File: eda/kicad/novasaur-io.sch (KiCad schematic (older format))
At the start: 67 parts, among them J1 POWER IN, J3 AUDIO OUT, J4 KEYBOARD, J5 SERIAL, J5 SPKR, J6 DISPLAY, J7 EXPANSION, J8 EXP OUT, Q1 2N3904, Q2 2N3904, Q4 BS270, U1 74F86, U2 74F08, U38 74HCT4053, U39 MAX232, U4 74F32, U40 NJM4580, U41 LM2576, U6 74ALS139, U7 74ALS139

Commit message: final rev5 update before removing buck reg
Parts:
- RN7, RN8: footprint Resistor_THT:R_Array_SIP8 -> Resistor_THT:R_Array_SIP9; symbol Device:R_Network07_US -> Device:R_Network08_US
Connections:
- wire segments 351 -> 353
- no-connect marks 9 -> 11
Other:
- moved on the sheet: RN9
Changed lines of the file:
@@
 L Device:R_Pack03_SIP RN?
 U 1 1 5F52EE33
-P 4300 3800
+P 4300 3900
 AR Path="/5DAA3954/5F52EE33" Ref="RN?"  Part="1"
 AR Path="/5F52EE33" Ref="RN?"  Part="1"
@@
 AR Path="/5DA1E9BD/5F52EE33" Ref="RN?"  Part="1"
 AR Path="/5DA1E9C0/5F52EE33" Ref="RN9"  Part="1"
-F 0 "RN9" V 3750 3750 50  0000 L CNN
-F 1 "220" V 3850 3750 50  0000 L CNN
-F 2 "Resistor_THT:R_Array_SIP6" V 4875 3800 50  0001 C CNN
-F 3 "http://www.vishay.com/docs/31509/csc.pdf" H 4300 3800 50  0001 C CNN
-	1    4300 3800
+F 0 "RN9" V 3750 3850 50  0000 L CNN
+F 1 "220" V 3850 3850 50  0000 L CNN
+F 2 "Resistor_THT:R_Array_SIP6" V 4875 3900 50  0001 C CNN
+F 3 "http://www.vishay.com/docs/31509/csc.pdf" H 4300 3900 50  0001 C CNN
+	1    4300 3900
 	0    -1   1    0
 $EndComp
 Wire Wire Line
-	4550 2650 4450 2650
-Wire Wire Line
-	4550 2550 4450 2550
-Wire Wire Line
-	4450 2950 4550 2950
-Wire Wire Line
-	4550 2850 4450 2850
+	4550 2700 4450 2700
+Wire Wire Line
+	4550 2600 4450 2600
+Wire Wire Line
+	4450 3000 4550 3000
+Wire Wire Line
+	4550 2900 4450 2900
 Wire Wire Line
 	4550 1500 4450 1500
@@
 	4450 1900 4550 1900
 Wire Wire Line
-	4550 2650 4550 2600
+	4550 2700 4550 2650
 Wire Wire Line
 	4450 1800 4550 1800
 Wire Wire Line
+	4500 4000 4550 4000
+Wire Wire Line
+	4550 4000 4550 4200
+Wire Wire Line
+	4550 4200 4500 4200
+Wire Wire Line
 	4500 3900 4550 3900
 Wire Wire Line
-	4550 3900 4550 4100
-Wire Wire Line
-	4550 4100 4500 4100
-Wire Wire Line
-	4500 3800 4550 3800
-Wire Wire Line
-	4500 3600 4550 3600
-Wire Wire Line
-	4550 3600 4550 3800
-Text Label 4600 3500 0    50   ~ 0
+	4500 3700 4550 3700
+Wire Wire Line
+	4550 3700 4550 3900
+Text Label 4600 3600 0    50   ~ 0
 C6
-Text Label 4600 4200 0    50   ~ 0
+Text Label 4600 4300 0    50   ~ 0
 C7
 Text Label 4600 1400 0    50   ~ 0
@@
 Text Label 4600 1700 0    50   ~ 0
 C2
-Text Label 4600 2450 0    50   ~ 0
+Text Label 4600 2500 0    50   ~ 0
 C3
-Text Label 4600 2600 0    50   ~ 0
+Text Label 4600 2650 0    50   ~ 0
 C4
-Text Label 4600 2750 0    50   ~ 0
+Text Label 4600 2800 0    50   ~ 0
 C5
 Wire Wire Line
@@
 Wire Wire Line
 	4550 1550 4550 1500
-Connection ~ 4550 2600
-Wire Wire Line
-	4550 2600 4550 2550
-Wire Wire Line
-	4550 2850 4550 2950
-Wire Wire Line
-	4550 2850 4550 2750
-Connection ~ 4550 2850
-Wire Wire Line
-	4450 3050 4550 3050
-Wire Wire Line
-	4550 3050 4550 2950
-Connection ~ 4550 2950
-Wire Wire Line
-	4700 3500 4500 3500
-Wire Wire Line
-	4700 4200 4500 4200
+Connection ~ 4550 2650
+Wire Wire Line
+	4550 2650 4550 2600
+Wire Wire Line
+	4550 2900 4550 3000
+Wire Wire Line
+	4550 2900 4550 2800
+Connection ~ 4550 2900
+Wire Wire Line
+	4450 3100 4550 3100
+Wire Wire Line
+	4550 3100 4550 3000
+Connection ~ 4550 3000
+Wire Wire Line
+	4700 3600 4500 3600
+Wire Wire Line
+	4700 4300 4500 4300
 Wire Wire Line
 	4700 1550 4550 1550
@@
 	4700 1700 4550 1700
 Wire Wire Line
-	4700 2600 4550 2600
-Entry Wire Line
-	4700 3500 4800 3400
-Entry Wire Line
-	4700 4200 4800 4100
+	4700 2650 4550 2650
+Entry Wire Line
+	4700 3600 4800 3500
+Entry Wire Line
+	4700 4300 4800 4200
 Entry Wire Line
 	4800 1450 4700 1550
@@
 	4800 1600 4700 1700
 Entry Wire Line
-	4800 2350 4700 2450
-Entry Wire Line
-	4800 2650 4700 2750
-Entry Wire Line
-	4800 2500 4700 2600
-Connection ~ 4550 4100
+	4800 2400 4700 2500
+Entry Wire Line
+	4800 2700 4700 2800
+Entry Wire Line
+	4800 2550 4700 2650
+Connection ~ 4550 4200
 Text GLabel 4800 1100 1    50   Input ~ 0
 C[0..7]
@@
 	4450 1400 4700 1400
 Wire Wire Line
-	4450 2450 4700 2450
-Wire Wire Line
-	4550 2750 4700 2750
+	4450 2500 4700 2500
+Wire Wire Line
+	4550 2800 4700 2800
 Wire Wire Line
 	4450 1700 4550 1700
 Connection ~ 4550 1700
 Wire Wire Line
-	4450 2750 4550 2750
-Connection ~ 4550 2750
+	4450 2800 4550 2800
+Connection ~ 4550 2800
 $Comp
 L power:GNDD #PWR?
@@
 	8250 4350 8250 4100
 $Comp
-L Device:R_Network07_US RN?
+L Device:R_Network08_US RN?
 U 1 1 5DF0AA91
-P 4250 1700
+P 4250 1800
 AR Path="/5DAA3954/5DF0AA91" Ref="RN?"  Part="1"
 AR Path="/5DAA5CD8/5D9A6C5F/5DF0AA91" Ref="RN?"  Part="1"
 AR Path="/5DA1E9BD/5DF0AA91" Ref="RN?"  Part="1"
 AR Path="/5DA1E9C0/5DF0AA91" Ref="RN7"  Part="1"
-F 0 "RN7" V 3700 1600 50  0000 L CNN
-F 1 "1k" V 3800 1650 50  0000 L CNN
-F 2 "Resistor_THT:R_Array_SIP8" V 4725 1700 50  0001 C CNN
-F 3 "http://www.vishay.com/docs/31509/csc.pdf" H 4250 1700 50  0001 C CNN
-	1    4250 1700
+F 0 "RN7" V 3600 1700 50  0000 L CNN
+F 1 "1k" V 3700 1750 50  0000 L CNN
+F 2 "Resistor_THT:R_Array_SIP9" V 4725 1800 50  0001 C CNN
+F 3 "http://www.vishay.com/docs/31509/csc.pdf" H 4250 1800 50  0001 C CNN
+	1    4250 1800
 	0    -1   1    0
 $EndComp
 $Comp
-L Device:R_Network07_US RN?
+L Device:R_Network08_US RN?
 U 1 1 5DF28750
-P 4250 2750
+P 4250 2900
 AR Path="/5DAA3954/5DF28750" Ref="RN?"  Part="1"
 AR Path="/5DAA5CD8/5D9A6C5F/5DF28750" Ref="RN?"  Part="1"
 AR Path="/5DA1E9BD/5DF28750" Ref="RN?"  Part="1"
 AR Path="/5DA1E9C0/5DF28750" Ref="RN8"  Part="1"
-F 0 "RN8" V 3700 2650 50  0000 L CNN
-F 1 "1k" V 3800 2700 50  0000 L CNN
-F 2 "Resistor_THT:R_Array_SIP8" V 4725 2750 50  0001 C CNN
-F 3 "http://www.vishay.com/docs/31509/csc.pdf" H 4250 2750 50  0001 C CNN
-	1    4250 2750
+F 0 "RN8" V 3600 2800 50  0000 L CNN
+F 1 "1k" V 3700 2850 50  0000 L CNN
+F 2 "Resistor_THT:R_Array_SIP9" V 4725 2900 50  0001 C CNN
+F 3 "http://www.vishay.com/docs/31509/csc.pdf" H 4250 2900 50  0001 C CNN
+	1    4250 2900
 	0    -1   1    0
 $EndComp
@@
 	3900 6650 4200 6650
 Wire Wire Line
-	4550 4100 4550 4350
-Wire Wire Line
-	4050 2450 3950 2450
+	4050 2500 3950 2500
 Wire Wire Line
 	4050 1400 3750 1400
@@
 	3600 3750 3750 3750
 Wire Wire Line
-	3600 4050 3950 4050
-Wire Wire Line
-	3600 4350 4550 4350
-Wire Wire Line
-	3950 2450 3950 4050
+	3950 2500 3950 4050
 Wire Wire Line
 	1600 2400 1650 2400
@@
 	8000 1050 8200 1050
 Connection ~ 8000 1300
+NoConn ~ 4450 2100
+NoConn ~ 4450 3200
+Wire Wire Line
+	3600 4050 3950 4050
+Wire Wire Line
+	3950 4350 3600 4350
+Wire Wire Line
+	3950 4550 4550 4550
+Wire Wire Line
+	4550 4200 4550 4550
+Wire Wire Line
+	3950 4350 3950 4550
 Wire Bus Line
 	4300 6750 4300 7050
@@
 	4950 1100 4950 2000
 Wire Bus Line
-	4800 1100 4800 4100
+	2850 1400 2850 2200
 Wire Bus Line
-	2850 1400 2850 2200
+	4800 1100 4800 4200
 $EndSCHEMATC

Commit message: rev5 schematic
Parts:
- removed C13: 1000u, Capacitor_THT:CP_Radial_D10.0mm_P5.00mm, symbol Device:CP1
- removed C23: 100u, Capacitor_THT:CP_Radial_D8.0mm_P3.50mm, symbol Device:CP1
- removed D3: 1N5822, Diode_THT:D_DO-201AD_P5.08mm_Vertical_AnodeUp, symbol Device:D_Schottky_ALT
- removed L1: 180uH, Inductor_THT:L_Radial_D12.5mm_P7.00mm_Fastron_09HCP, symbol Device:L_Core_Ferrite
- removed TP35: +24v, TestPoint:TestPoint_THTPad_1.0x1.0mm_Drill0.5mm, symbol Connector:TestPoint_Alt
- removed U41: LM2576, Package_TO_SOT_THT:TO-220-5_P3.4x3.7mm_StaggerOdd_Lead3.8mm_Vertical, symbol Regulator_Switching:LM2576HVT-5
- added C22, C23: 4.7u, Capacitor_THT:C_Disc_D6.0mm_W4.4mm_P5.00mm, symbol Device:C
- added U41: MCP1827S, Package_TO_SOT_THT:TO-220-3_Horizontal_TabDown, symbol Regulator_Linear:MCP1826S
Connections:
- net labels removed: +24V
- wire segments 353 -> 338
- no-connect marks 11 -> 12
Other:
- moved on the sheet: C1, C2, C3, C4, C5, J1, TP33, TP34, U1E, U2E, U3E, U4C

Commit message: rev 1.6 schematic
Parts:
- U41: footprint Package_TO_SOT_THT:TO-220-3_Horizontal_TabDown -> Package_TO_SOT_THT:TO-220-5_P3.4x3.8mm_StaggerOdd_Lead7.13mm_TabDown; symbol Regulator_Linear:MCP1826S -> Regulator_Linear:LP3963-3.3
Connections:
- net labels added: ~reset
- wire segments 338 -> 339
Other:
- moved on the sheet: C1, C2, C22, C23, C3, C4, C5, J1, TP33, TP34

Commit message: rename P reg to T
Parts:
- C22: renamed from C23; value 4.7u -> 1u; footprint Capacitor_THT:C_Disc_D6.0mm_W4.4mm_P5.00mm -> Capacitor_THT:C_Disc_D5.1mm_W3.2mm_P5.00mm
- C23: renamed from C22; value 4.7u -> 22u; footprint Capacitor_THT:C_Disc_D6.0mm_W4.4mm_P5.00mm -> Capacitor_THT:CP_Radial_D6.3mm_P2.50mm; symbol Device:C -> Device:CP1
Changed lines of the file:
@@
 Sheet 4 4
 Title "Input & Output"
-Date "2020-03-08"
+Date "2020-03-29"
 Rev "1.6"
 Comp ""
@@
 AR Path="/5DAA5CD8/5D9AFF37/630964B4" Ref="C?"  Part="1"
 AR Path="/5DA1E9C0/630964B4" Ref="C19"  Part="1"
-F 0 "C19" H 7100 2150 50  0000 C CNN
-F 1 "330p" H 7100 2050 50  0000 C CNN
+F 0 "C19" H 7150 2150 50  0000 C CNN
+F 1 "330p" H 7150 2050 50  0000 C CNN
 F 2 "Capacitor_THT:C_Disc_D3.0mm_W2.0mm_P2.50mm" H 6938 1950 50  0001 C CNN
 F 3 "~" H 6900 2100 50  0001 C CNN
@@
 AR Path="/5DAA5CD8/5D9AFF37/5EAB34C5" Ref="C?"  Part="1"
 AR Path="/5DA1E9C0/5EAB34C5" Ref="C18"  Part="1"
-F 0 "C18" H 6300 2150 50  0000 C CNN
-F 1 "330p" H 6300 2050 50  0000 C CNN
+F 0 "C18" H 6350 2150 50  0000 C CNN
+F 1 "330p" H 6350 2050 50  0000 C CNN
 F 2 "Capacitor_THT:C_Disc_D3.0mm_W2.0mm_P2.50mm" H 6138 1950 50  0001 C CNN
 F 3 "~" H 6100 2100 50  0001 C CNN
@@
 AR Path="/5DAA5CD8/5D9AFF37/5E5DCFF5" Ref="R?"  Part="1"
 AR Path="/5DA1E9C0/5E5DCFF5" Ref="R8"  Part="1"
-F 0 "R8" H 8500 2100 50  0000 L CNN
+F 0 "R8" H 8550 2100 50  0000 L CNN
 F 1 "100k" H 8500 2000 50  0000 L CNN
 F 2 "Resistor_THT:R_Axial_DIN0204_L3.6mm_D1.6mm_P7.62mm_Horizontal" V 8440 2040 50  0001 C CNN
@@
 	9050 4100 9050 4350
 $Comp
-L Device:C C?
+L Device:CP1 C?
 U 1 1 5E710149
 P 7050 3650
 AR Path="/62D13D9D/5E710149" Ref="C?"  Part="1"
 AR Path="/5DAA5CD8/5D9AFF37/5E710149" Ref="C?"  Part="1"
-AR Path="/5DA1E9C0/5E710149" Ref="C22"  Part="1"
-F 0 "C22" H 7165 3696 50  0000 L CNN
-F 1 "4.7u" H 7165 3605 50  0000 L CNN
-F 2 "Capacitor_THT:C_Disc_D6.0mm_W4.4mm_P5.00mm" H 7088 3500 50  0001 C CNN
+AR Path="/5DA1E9C0/5E710149" Ref="C23"  Part="1"
+F 0 "C23" H 7165 3696 50  0000 L CNN
+F 1 "22u" H 7165 3605 50  0000 L CNN
+F 2 "Capacitor_THT:CP_Radial_D6.3mm_P2.50mm" H 7088 3500 50  0001 C CNN
 F 3 "~" H 7050 3650 50  0001 C CNN
 	1    7050 3650
@@
 AR Path="/62D13D9D/5E72DE16" Ref="C?"  Part="1"
 AR Path="/5DAA5CD8/5D9AFF37/5E72DE16" Ref="C?"  Part="1"
-AR Path="/5DA1E9C0/5E72DE16" Ref="C23"  Part="1"
-F 0 "C23" H 8765 3696 50  0000 L CNN
-F 1 "4.7u" H 8765 3605 50  0000 L CNN
-F 2 "Capacitor_THT:C_Disc_D6.0mm_W4.4mm_P5.00mm" H 8688 3500 50  0001 C CNN
+AR Path="/5DA1E9C0/5E72DE16" Ref="C22"  Part="1"
+F 0 "C22" H 8765 3696 50  0000 L CNN
+F 1 "1u" H 8765 3605 50  0000 L CNN
+F 2 "Capacitor_THT:C_Disc_D5.1mm_W3.2mm_P5.00mm" H 8688 3500 50  0001 C CNN
 F 3 "~" H 8650 3650 50  0001 C CNN
 	1    8650 3650

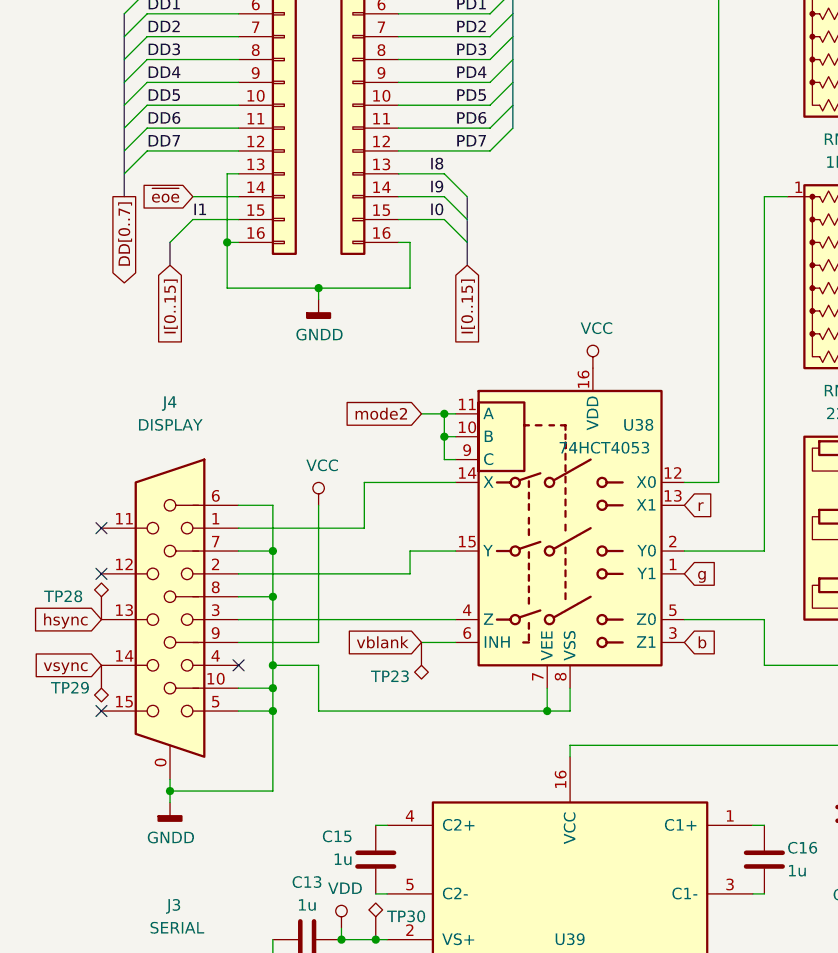
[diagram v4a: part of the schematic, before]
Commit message: add video headers
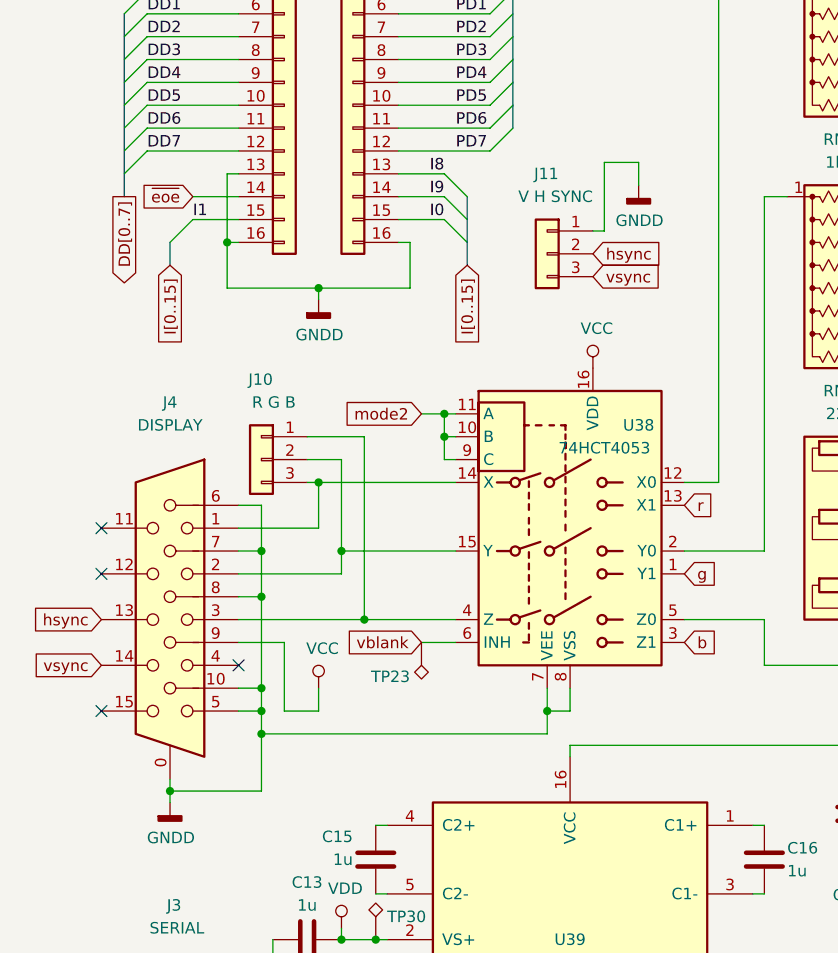
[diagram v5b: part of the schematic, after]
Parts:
- removed TP28: HSYNC, TestPoint:TestPoint_Pad_1.0x1.0mm, symbol Connector:TestPoint_Alt
- removed TP29: VSYNC, TestPoint:TestPoint_Pad_1.0x1.0mm, symbol Connector:TestPoint_Alt
- added J10: R G B, Connector_PinHeader_2.54mm:PinHeader_1x03_P2.54mm_Vertical, symbol Connector_Generic:Conn_01x03
- added J11: V H SYNC, Connector_PinHeader_2.54mm:PinHeader_1x03_P2.54mm_Vertical, symbol Connector_Generic:Conn_01x03
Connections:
- net GNDD: now also J11.1 (Pin_1)
- net hsync: now also J11.2 (Pin_2)
- net vsync: now also J11.3 (Pin_3)
- net at J6.1, U38.14 (X): now also J10.3 (Pin_3)
- net at J6.2, U38.15 (Y): now also J10.2 (Pin_2)
- net at J6.3, U38.4 (Z): now also J10.1 (Pin_1)
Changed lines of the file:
@@
 encoding utf-8
 Sheet 4 4
-Title "Input & Output"
-Date "2020-03-29"
+Title "Novasaur Retrocomputer"
+Date "2020-03-31"
 Rev "1.6"
 Comp ""
@@
 L power:VCC #PWR0115
 U 1 1 5D70CEC0
-P 2000 3850
+P 2000 4650
 AR Path="/62D13D9D/5D70CEC0" Ref="#PWR0115"  Part="1"
 AR Path="/5DAA5CD8/5D9AFF37/5D70CEC0" Ref="#PWR?"  Part="1"
 AR Path="/5DA1E9C0/5D70CEC0" Ref="#PWR0185"  Part="1"
-F 0 "#PWR0185" H 2000 3700 50  0001 C CNN
-F 1 "VCC" H 2017 4023 50  0000 C CNN
-F 2 "" H 2000 3850 50  0001 C CNN
-F 3 "" H 2000 3850 50  0001 C CNN
-	1    2000 3850
-	1    0    0    -1
-$EndComp
-Wire Wire Line
-	1650 4150 2400 4150
+F 0 "#PWR0185" H 2000 4500 50  0001 C CNN
+F 1 "VCC" H 2017 4823 50  0000 C CNN
+F 2 "" H 2000 4650 50  0001 C CNN
+F 3 "" H 2000 4650 50  0001 C CNN
+	1    2000 4650
+	1    0    0    -1
+$EndComp
 $Comp
 L Connector:DB15_Female_HighDensity_MountingHoles J6
@@
 	-1   0    0    -1
 $EndComp
-Wire Wire Line
-	1650 3950 2200 3950
 $Comp
 L Connector_Generic:Conn_01x16 J8
@@
 	2350 2300 2750 2300
 Wire Wire Line
-	2400 4150 2400 4050
-Wire Wire Line
-	2400 4050 2600 4050
-Wire Wire Line
-	2200 3950 2200 3750
-Wire Wire Line
-	2200 3750 2600 3750
-Wire Wire Line
 	1600 1200 1600 1100
 Wire Wire Line
@@
 Text GLabel 2450 3450 0    50   Input ~ 0
 mode2
-Connection ~ 2550 3450
 $Comp
 L Connector_Generic:Conn_01x16 J7
@@
 	1    0    0    -1
 $EndComp
-Wire Wire Line
-	2450 3450 2550 3450
 Wire Wire Line
 	1600 2700 1650 2700
@@
 	2050 6050 2100 6050
 Wire Wire Line
-	1650 4350 2600 4350
-Wire Wire Line
-	1650 3850 1800 3850
-Wire Wire Line
-	1650 4050 1800 4050
-Wire Wire Line
-	1650 4250 1800 4250
-Wire Wire Line
-	1650 4650 1800 4650
-Wire Wire Line
-	1650 4750 1800 4750
+	1650 3850 1750 3850
+Wire Wire Line
+	1650 4050 1750 4050
+Wire Wire Line
+	1650 4250 1750 4250
+Wire Wire Line
+	1650 4650 1750 4650
+Wire Wire Line
+	1650 4750 1750 4750
 Wire Wire Line
 	1350 5050 1350 5100
@@
 Wire Wire Line
 	1350 5100 1350 5150
-Wire Wire Line
-	1800 5100 1800 4750
-Wire Wire Line
-	1800 5100 1350 5100
-Connection ~ 1800 4750
-Wire Wire Line
-	1800 4650 1800 4550
-Connection ~ 1800 4650
-Connection ~ 1800 4250
-Wire Wire Line
-	1800 4250 1800 4050
-Connection ~ 1800 4050
-Wire Wire Line
-	1800 4050 1800 3850
-Wire Wire Line
-	1800 4750 1800 4650
-Wire Wire Line
-	1800 4550 2000 4550
-Connection ~ 1800 4550
-Wire Wire Line
-	1800 4250 1800 4550
-Wire Wire Line
-	2000 4750 3000 4750
 Connection ~ 3000 4750
 Wire Wire Line
@@
 Wire Wire Line
 	3000 4650 3000 4750
-Wire Wire Line
-	2000 4550 2000 4750
 $Comp
 L Device:C C?
@@
 Wire Wire Line
 	2100 6050 2250 6050
-$Comp
-L Connector:TestPoint_Alt TP?
-U 1 1 5E74D438
-P 1050 4350
-AR Path="/5E74D438" Ref="TP?"  Part="1"
-AR Path="/5DA1E9BA/5E74D438" Ref="TP?"  Part="1"
-AR Path="/5DA1E9BD/5E74D438" Ref="TP?"  Part="1"
-AR Path="/5DA1E9C0/5E74D438" Ref="TP28"  Part="1"
-F 0 "TP28" H 800 4450 50  0000 L CNN
-F 1 "HSYNC" H 800 4500 50  0001 L CNN
-F 2 "TestPoint:TestPoint_Pad_1.0x1.0mm" H 1250 4350 50  0001 C CNN
-F 3 "~" H 1250 4350 50  0001 C CNN
-	1    1050 4350
-	1    0    0    -1
-$EndComp
 Wire Wire Line
 	2300 5750 2250 5750
@@
 Wire Wire Line
 	6250 5000 6250 4900
-Wire Wire Line
-	2000 4450 2000 3850
-Wire Wire Line
-	1650 4450 2000 4450
 Entry Wire Line
 	1150 1400 1250 1500
@@
 	1250 1500 1650 1500
 $Comp
-L Connector:TestPoint_Alt TP?
-U 1 1 5E6FA207
-P 1050 4550
-AR Path="/5E6FA207" Ref="TP?"  Part="1"
-AR Path="/5DA1E9BA/5E6FA207" Ref="TP?"  Part="1"
-AR Path="/5DA1E9BD/5E6FA207" Ref="TP?"  Part="1"
-AR Path="/5DA1E9C0/5E6FA207" Ref="TP29"  Part="1"
-F 0 "TP29" H 1100 4650 50  0000 L CNN
-F 1 "VSYNC" H 800 4700 50  0001 L CNN
-F 2 "TestPoint:TestPoint_Pad_1.0x1.0mm" H 1250 4550 50  0001 C CNN
-F 3 "~" H 1250 4550 50  0001 C CNN
-	1    1050 4550
-	-1   0    0    1
-$EndComp
-$Comp
 L Transistor_BJT:2N3904 Q1
 U 1 1 5E7F79E8
@@
 Text GLabel 7450 3300 0    50   Output ~ 0
 ~reset
+$Comp
+L Connector_Generic:Conn_01x03 J10
+U 1 1 5E8D84F1
+P 1750 3650
+AR Path="/5DA1E9C0/5E8D84F1" Ref="J10"  Part="1"
+AR Path="/5E8D84F1" Ref="J?"  Part="1"
+F 0 "J10" H 1700 4000 50  0000 L CNN
+F 1 "R  G  B" H 1600 3900 50  0000 L CNN
+F 2 "Connector_PinHeader_2.54mm:PinHeader_1x03_P2.54mm_Vertical" H 1750 3650 50  0001 C CNN
+F 3 "~" H 1750 3650 50  0001 C CNN
+	1    1750 3650
+	-1   0    0    -1
+$EndComp
+Wire Wire Line
+	3000 4850 3000 4750
+Wire Wire Line
+	2550 3450 2450 3450
+Connection ~ 2550 3450
+Wire Wire Line
+	1650 4350 2200 4350
+Wire Wire Line
+	1650 3950 2000 3950
+Wire Wire Line
+	1650 4150 2100 4150
+Wire Wire Line
+	2000 3750 2000 3950
+Wire Wire Line
+	2000 3750 2600 3750
+Wire Wire Line
+	1950 3550 2200 3550
+Wire Wire Line
+	1950 3650 2100 3650
+Wire Wire Line
+	1950 3750 2000 3750
+Connection ~ 2000 3750
+Wire Wire Line
+	1750 3850 1750 4050
+Connection ~ 1750 4050
+Wire Wire Line
+	1750 4050 1750 4250
+Connection ~ 1750 4250
+Wire Wire Line
+	1750 4250 1750 4650
+Connection ~ 1750 4650
+Wire Wire Line
+	1750 4650 1750 4750
+Connection ~ 1750 4750
+Wire Wire Line
+	1750 4750 1750 4850
+Wire Wire Line
+	1750 4850 1750 5100
+Connection ~ 1750 4850
+Wire Wire Line
+	1750 5100 1350 5100
+Wire Wire Line
+	1750 4850 3000 4850
+Wire Wire Line
+	1650 4450 1850 4450
+Wire Wire Line
+	2100 3650 2100 4050
+Connection ~ 2100 4050
+Wire Wire Line
+	2100 4050 2100 4150
+Wire Wire Line
+	2100 4050 2600 4050
+Wire Wire Line
+	2200 3550 2200 4350
+Connection ~ 2200 4350
+Wire Wire Line
+	2200 4350 2600 4350
+Wire Wire Line
+	1850 4750 2000 4750
+Wire Wire Line
+	2000 4750 2000 4650
+Wire Wire Line
+	1850 4450 1850 4750
+Text GLabel 3200 2850 2    50   Input ~ 0
+vsync
+Text GLabel 3200 2750 2    50   Input ~ 0
+hsync
+Wire Wire Line
+	3400 2350 3400 2450
+$Comp
+L power:GNDD #PWR?
+U 1 1 5F8B73E5
+P 3400 2450
+AR Path="/62D13D9D/5F8B73E5" Ref="#PWR?"  Part="1"
+AR Path="/5DAA5CD8/5D9AFF37/5F8B73E5" Ref="#PWR?"  Part="1"
+AR Path="/5DA1E9C0/5F8B73E5" Ref="#PWR0181"  Part="1"
+F 0 "#PWR0181" H 3400 2200 50  0001 C CNN
+F 1 "GNDD" H 3404 2295 50  0000 C CNN
+F 2 "" H 3400 2450 50  0001 C CNN
+F 3 "" H 3400 2450 50  0001 C CNN
+	1    3400 2450
+	1    0    0    -1
+$EndComp
+Wire Wire Line
+	3200 2650 3250 2650
+Wire Wire Line
+	3250 2350 3400 2350
+Wire Wire Line
+	3250 2650 3250 2350
+$Comp
+L Connector_Generic:Conn_01x03 J11
+U 1 1 5F873810
+P 3000 2750
+AR Path="/5DA1E9C0/5F873810" Ref="J11"  Part="1"
+AR Path="/5F873810" Ref="J?"  Part="1"
+F 0 "J11" H 2950 3100 50  0000 L CNN
+F 1 "V  H SYNC" H 2800 3000 50  0000 L CNN
+F 2 "Connector_PinHeader_2.54mm:PinHeader_1x03_P2.54mm_Vertical" H 3000 2750 50  0001 C CNN
+F 3 "~" H 3000 2750 50  0001 C CNN
+	1    3000 2750
+	-1   0    0    -1
+$EndComp
 Wire Bus Line
 	4300 6750 4300 7050

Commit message: power sw + super caps
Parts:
- added C24, C25, C26, C27: 2F, Capacitor_THT:CP_Radial_D8.0mm_P3.50mm, symbol Device:CP1
- added D3: BAT42, Diode_THT:D_DO-35_SOD27_P7.62mm_Horizontal, symbol Device:D_Schottky_ALT
- added R10, R9: 100k, Resistor_THT:R_Axial_DIN0204_L3.6mm_D1.6mm_P7.62mm_Horizontal, symbol Device:R_US
- added SW1: POWER, Button_Switch_THT:SW-PBH2U, symbol Switch:SW_Push_DPDT
- renumbered J11 to J10, J10 to J9, R4 to R3, R5 to R4, R6 to R5, R7 to R6, R8 to R7, R9 to R8
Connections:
- net I0 is gone; now on net C0: J8.15 (Pin_15)
- net I1 is gone; now on net C1: J7.15 (Pin_15)
- net I3 is gone; now on net C3: J7.4 (Pin_4)
- net C0: no longer RN7.2 (R1)
- net C1: no longer RN7.3 (R2), RN7.4 (R3)
- net C3: no longer RN8.2 (R1)
- net GNDD: now also C3.1, J7.1 (Pin_1), J8.4 (Pin_4), C25.2, C27.2, SW1.3 (C), SW1.5 (B), SW1.6 (C); no longer C3.2, J7.16 (Pin_16)
- net VCC: now also C3.2, J7.16 (Pin_16), D3.2 (A), R9.2; no longer C3.1, J7.1 (Pin_1), J8.4 (Pin_4), U41.1 (~SHDN)
- net ~reset: now also R9.1
- net at C22.1, J1.1, U41.2 (IN): now also R10.1
- net C2 renamed T2
- net C4 renamed T4
- net C5 renamed T5
- net C6 renamed T6
- net C7 renamed T7
- net I8 renamed C8
- net I9 renamed C9
- net ~inoe renamed ~ioe
- new net: R10.2, SW1.4 (A), U41.1 (~SHDN)
- new net: C26.2, C27.1
- new net: C24.2, C25.1
- new net +BATT: C24.1, C26.1, D3.1 (K), SW1.1 (A)
- new net T0: RN7.2 (R1)
- new net T1: RN7.3 (R2), RN7.4 (R3)
- new net T3: RN8.2 (R1)
- new net ~dce: SW1.2 (B)
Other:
- moved on the sheet: C1, C2, C22, C23, C3, J1, J10, TP23, TP33, TP34, U41
